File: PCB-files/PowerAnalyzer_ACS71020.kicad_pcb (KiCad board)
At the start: 2 copper layers, 58.5 x 67.8 mm, 37 parts, among them J1 L_VinN_out, J2 L_VinL_out, J3 L_VinN_in, J4 H_VinL_in, J5 Conn_01x08, J6 Conn_01x06, M1 MountingHole_2.5mm, U1 UCC12040, U2 ACS71020, U3 Teensy4.0, U4 Si8641

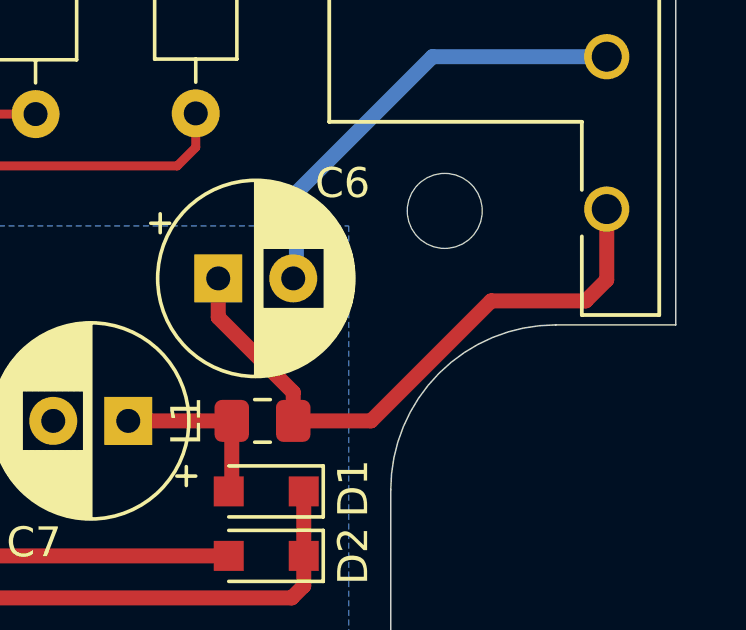
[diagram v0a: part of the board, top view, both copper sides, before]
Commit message: Added a watchdog timer
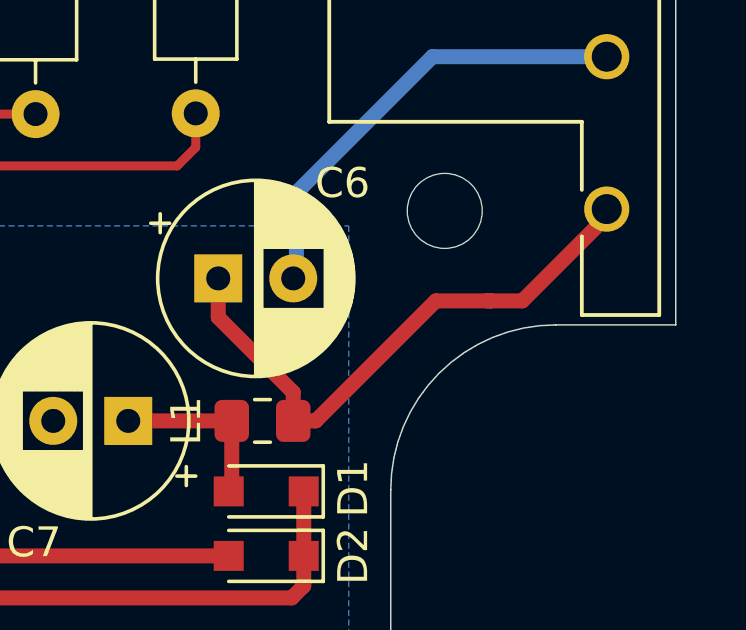
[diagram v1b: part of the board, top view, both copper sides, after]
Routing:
- net /5V(AC): track 20.5 -> 19.4 mm

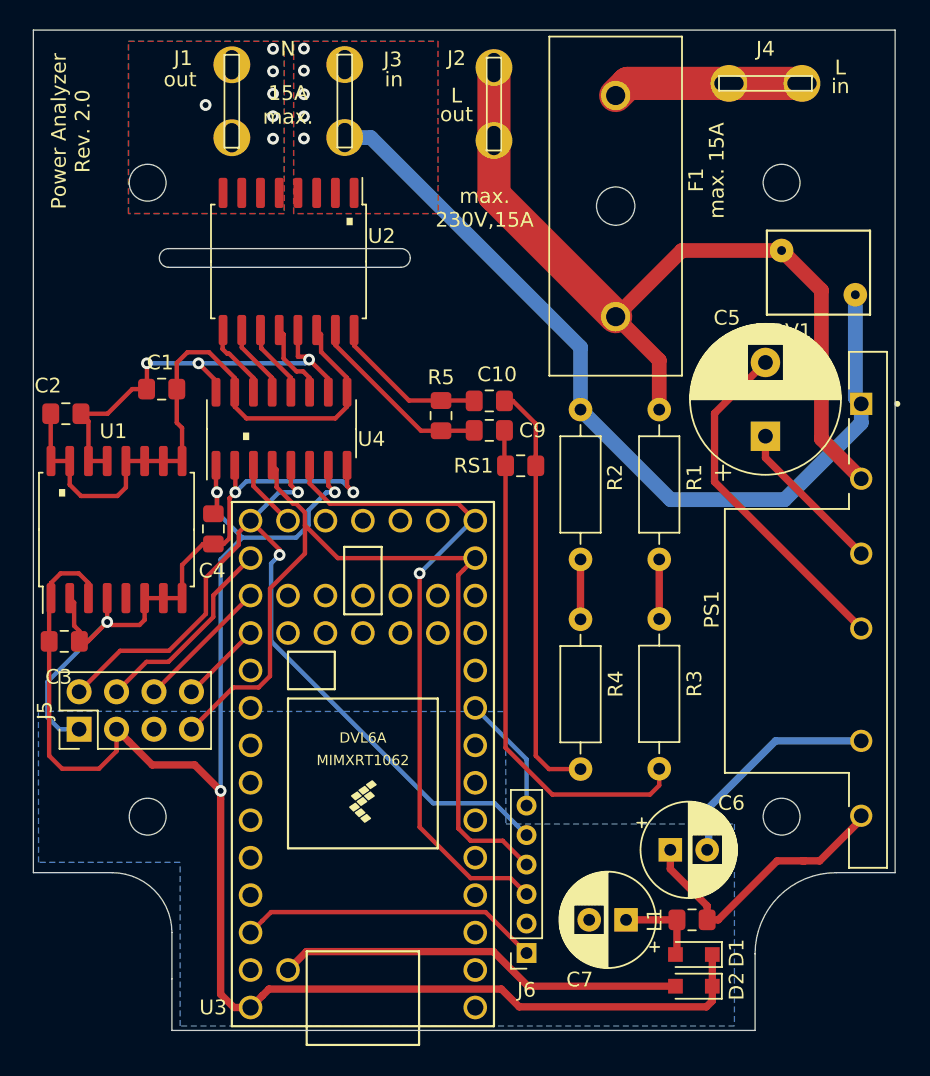
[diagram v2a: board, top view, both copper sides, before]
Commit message: PCB and Software Changes
PCB:
- Added a pads for pin-headers with 2.54mm pitch, for adding an external SD-card.
- Description for pins
- changed position of capacitors C1 to C4, in order to work correctly

Software:
- Added whole address R/W functions, to test the storage capabilities in the local EEPROM.
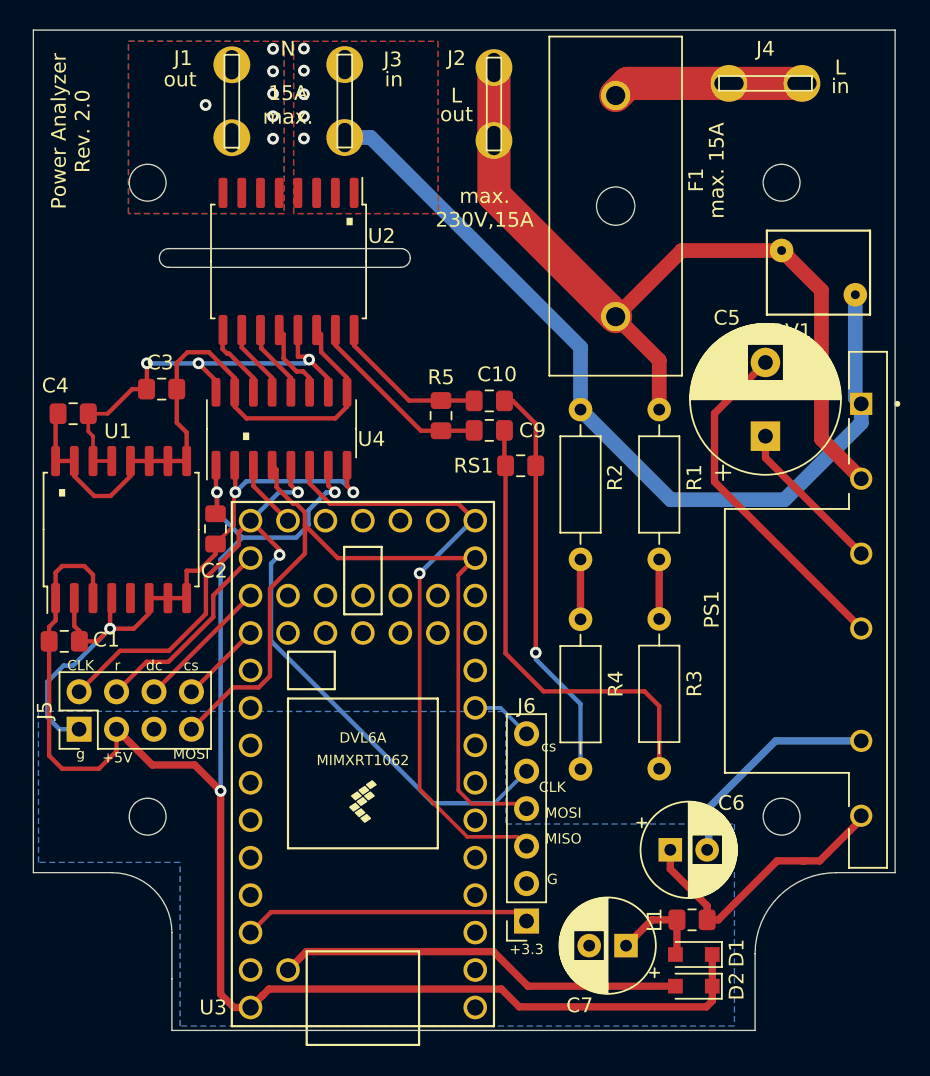
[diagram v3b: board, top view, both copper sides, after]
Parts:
- C1: renamed from C3; value 100p -> 100n
- C4: renamed from C2; value 100p -> 100n
- J6: footprint Connector_PinSocket_2.00mm:PinSocket_1x06_P2.00mm_Vertical -> Connector_PinSocket_2.54mm:PinSocket_1x06_P2.54mm_Vertical
- moved J6 2.17 mm to (100.0, 181.1)
- moved C7 1.75 mm to (106.8, 182.8)
- moved C4 0.50 mm to (69.2, 146.7)
- moved U1 0.31 mm to (72.5, 154.5)
- moved C2 0.14 mm to (78.9, 154.5)
- renumbered C4 to C2, C1 to C3
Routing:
- net CS_SD: track 8.07 -> 4.21 mm
- net Net-(C9-Pad1): track 34.7 -> 31.3 mm
- net MOSI: track 60.1 -> 57.0 mm
- net MISO: track 45.1 -> 42.3 mm
- net +5V: track 119.0 -> 120.3 mm
- net Net-(C10-Pad1): track 28.7 -> 27.4 mm, vias 0 -> 1
- net 3.3V: track 20.4 -> 19.5 mm
- net Net-(C7-Pad1): track 5.84 -> 6.57 mm
- net GNDS: track 44.1 -> 43.5 mm
- net /VISO: track 30.6 -> 30.0 mm
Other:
- board text added: "+3.3"
- board text added: "+5V"
- board text added: "CLK"
- board text added: "G"
- board text added: "MISO"
- board text added: "MOSI"
- board text added: "cs"
- board text added: "dc"
- board text added: "g"
- board text added: "r"

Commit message: PCB Updates
Mistakes in Pin-wiring corrected
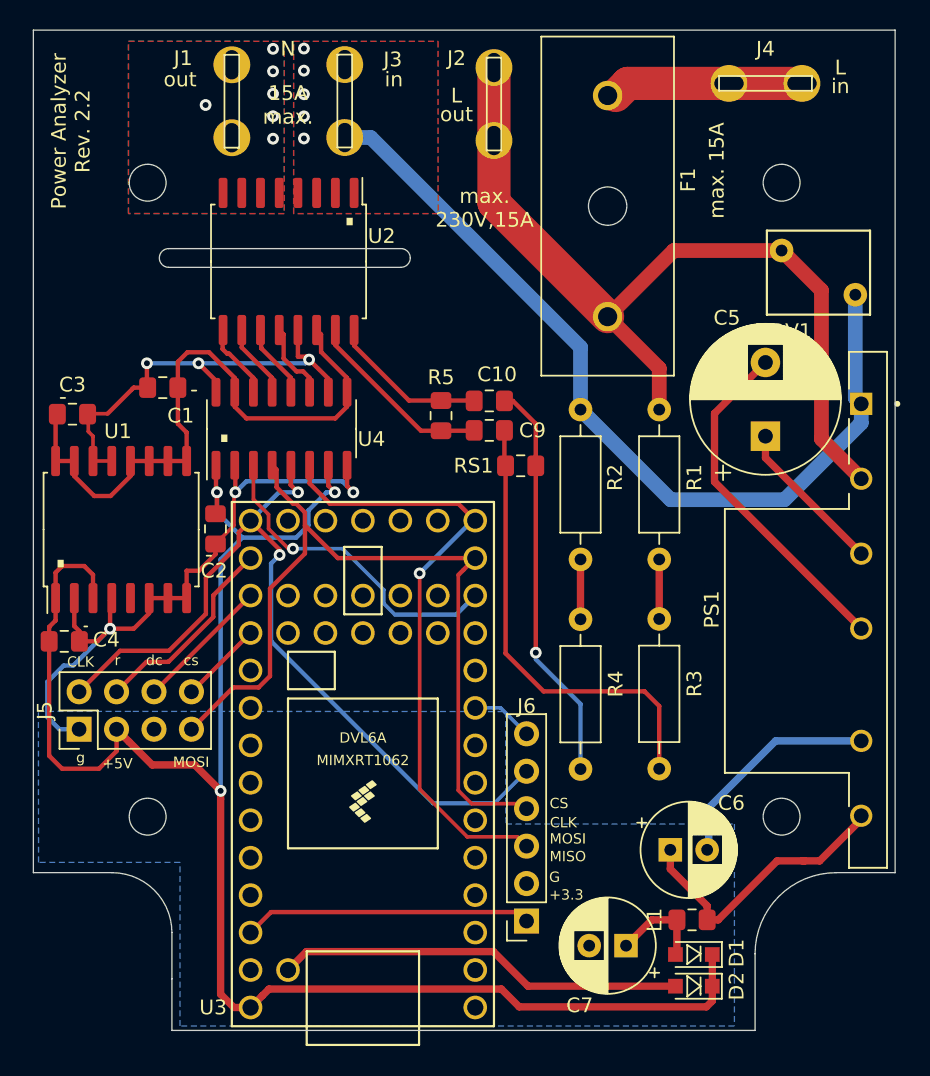
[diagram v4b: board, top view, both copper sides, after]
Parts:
- C2: value 10u -> 100n
- C4: renamed from C1; value 100n -> 10u
- moved C1 6.33 mm to (75.3, 144.9), turned to 180 degrees
- moved C3 6.28 mm to (69.2, 146.7), turned to 0 degrees
- moved F1 0.55 mm to (105.5, 132.6)
- renumbered C4 to C1
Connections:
- U3 pad 12: Net-(U3-Pad12) -> /CS1
- U3 pad 19: /CS1 -> Net-(U3-Pad19)
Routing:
- net /CS1: track 4.73 -> 22.2 mm, vias 0 -> 1
- net Net-(F1-Pad2): track 58.7 -> 59.2 mm
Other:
- board text added: "CS"
- board text added: "Power Analyzer Rev. 2.2"
- board text removed: "Power Analyzer Rev. 2.0"
